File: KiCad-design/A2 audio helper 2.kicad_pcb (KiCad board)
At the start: 2 copper layers, 45.5 x 65.5 mm, 34 parts, among them J1 PIN HEADER 1x2, J10 PIN HEADER 1x2, J11 PIN HEADER 1x3, J12 PIN HEADER 1x3, J13 PIN HEADER 1x3, J2 PIN HEADER 1x2, J3 PIN HEADER 1x2, J4 SJ1-3515N, J5 PIN HEADER 1x3, J6 PIN HEADER 1x3, J7 SJ1-3515N, J8 PIN HEADER 1x5, J9 PIN HEADER 1x2, K1 SR11-5V-200-2C, SW2 SW_DPDT_x2, U1 pam8403

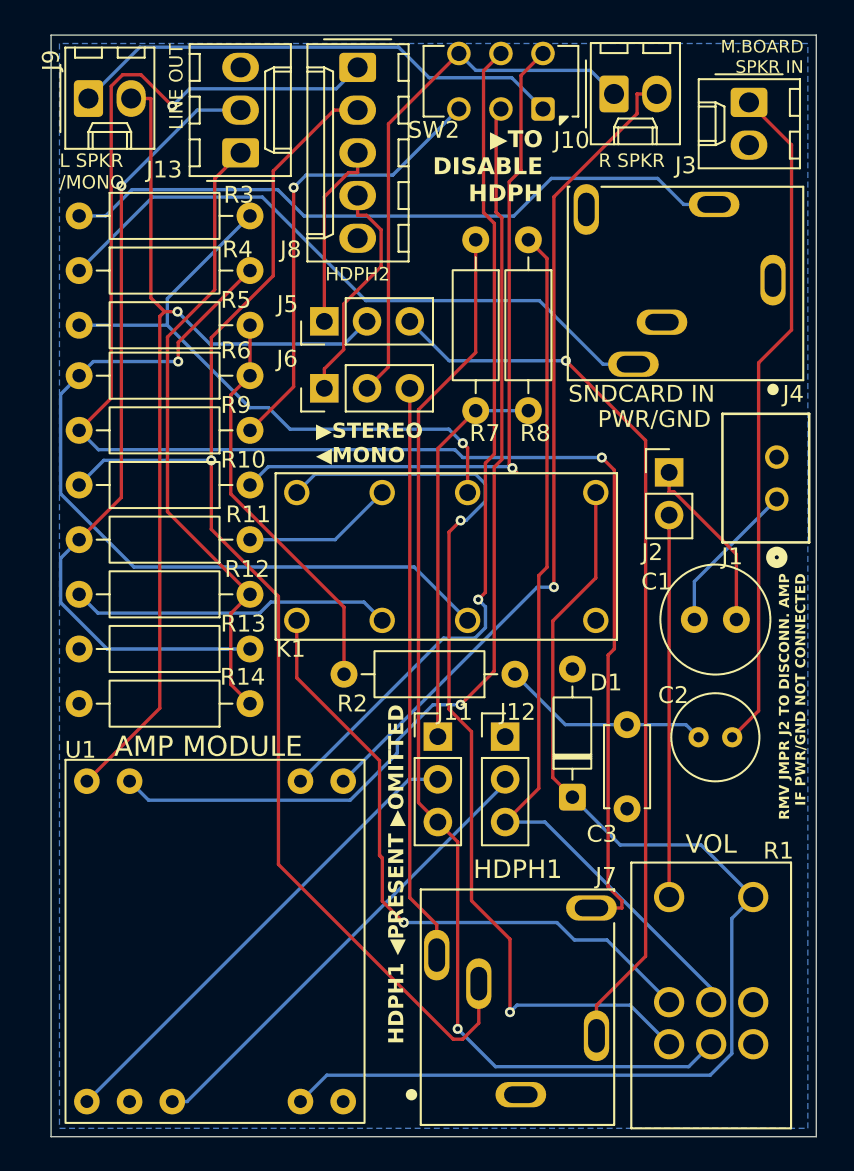
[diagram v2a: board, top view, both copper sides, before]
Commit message: ribbon cbl to remote vol & headph board
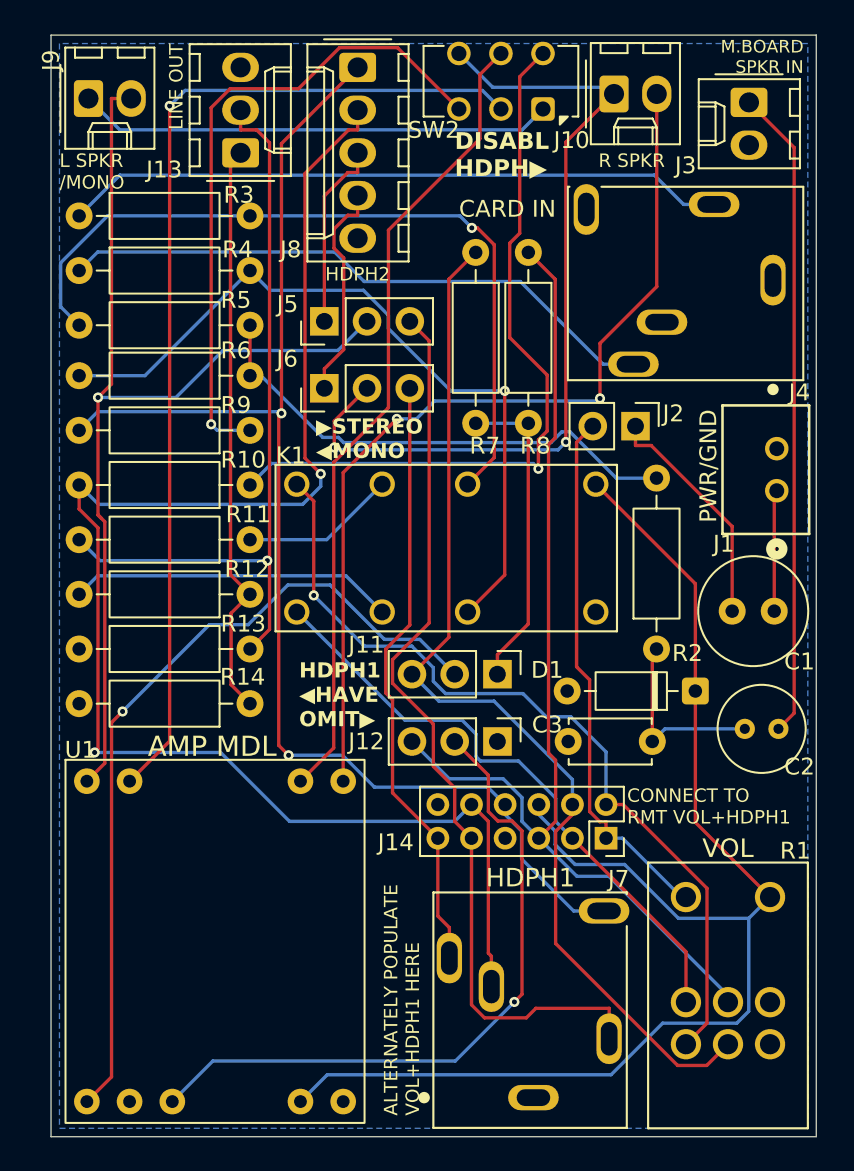
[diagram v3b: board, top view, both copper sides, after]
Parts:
- added J14: PIN HEADER 2x6, Connector_PinSocket_2.00mm:PinSocket_2x06_P2.00mm_Vertical, F.Cu at (83.0, 97.8)
- J1: footprint footprints:CONN_22035025_MOL -> Molex5267:CONN_22035025_MOL
- moved D1 9.66 mm to (88.3, 89.0), turned to 180 degrees
- moved R2 8.55 mm to (86.0, 86.5), turned to 90 degrees
- moved J11 5.13 mm to (76.5, 88.0), turned to -90 degrees
- moved C1 4.78 mm to (93.0, 84.2), turned to 180 degrees
- moved J2 3.40 mm to (84.8, 73.2), turned to -90 degrees
- moved C2 2.80 mm to (93.2, 91.2)
- moved C3 1.80 mm to (85.8, 92.0), turned to 180 degrees
- moved R1 1.00 mm to (90.2, 107.5)
- moved J7 0.77 mm to (78.7, 113.2)
- moved R7 0.75 mm to (75.2, 62.9)
- moved R8 0.75 mm to (78.4, 62.9)
- moved J12 0.54 mm to (76.5, 92.0), turned to -90 degrees
- moved J1 0.50 mm to (93.2, 77.1)
- moved K1 0.50 mm to (73.5, 80.5)
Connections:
- net /AMP_CONTROL renamed V_OUT
- net /HP1_IS_PRIMARY_L renamed HP1_TN
- net /HP1_IS_PRIMARY_R renamed HP1_RN
- net /HP_OUT_L renamed HP1_T
- net /HP_OUT_R renamed HP1_R
- net /VOLUME_ADJUSTED_L renamed VOL_L
- net /VOLUME_ADJUSTED_R renamed VOL_R
- net /VOLUME_SOURCE_L renamed SRC_L
- net /VOLUME_SOURCE_R renamed SRC_R
- net /V_IN_ENABLED renamed V_IN
- net GND renamed RMT_GND
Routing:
- net /AMP_INPUT_L: track 28.8 -> 49.1 mm, vias 0 -> 1
- net HP1_T: track 99.1 -> 79.5 mm
- net /RSPKR+: track 32.4 -> 50.5 mm, vias 0 -> 2
- net HP1_R: track 78.3 -> 91.9 mm, vias 1 -> 2
- net /AMP_INPUT_R: track 27.9 -> 40.6 mm, vias 0 -> 1
- net Net-(SW2A-C): track 27.3 -> 39.0 mm
- net V_OUT: track 69.5 -> 81.1 mm
- net /INPUT_AUDIO_L: track 37.3 -> 46.7 mm
- net V_IN: track 22.7 -> 32.0 mm
- net VOL_R: track 53.3 -> 62.5 mm
- net SRC_L: track 56.5 -> 49.7 mm, vias 2 -> 1
- net /AUDIO_MB_AC: track 24.0 -> 30.2 mm
- net /RSPKR-: track 49.9 -> 54.9 mm, vias 1 -> 2
- net /MONO_MIX_POINT: track 23.4 -> 18.8 mm
- net /LSPKR-: track 57.4 -> 60.8 mm
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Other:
- board text added: "ALTERNATELY POPULATE VOL+HDPH1 HERE"
- board text added: "AMP MDL"
- board text added: "CARD IN"
- board text added: "CONNECT TO RMT VOL+HDPH1"
- board text added: "HDPH1 ◀HAVE ︎OMIT▶"
- board text added: "︎︎DISABL HDPH▶"
- board text removed: "AMP MODULE"
- board text removed: "HDPH1 ◀︎PRESENT ▶︎OMITTED"
- board text removed: "RMV JMPR J2 TO DISCONN. AMP IF PWR/GND NOT CONNECTED"
- board text removed: "SNDCARD IN"
- board text removed: "▶︎︎TO DISABLE HDPH"

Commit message: desc'd ribbon conn better in schematic, fixed LSPKR+ error
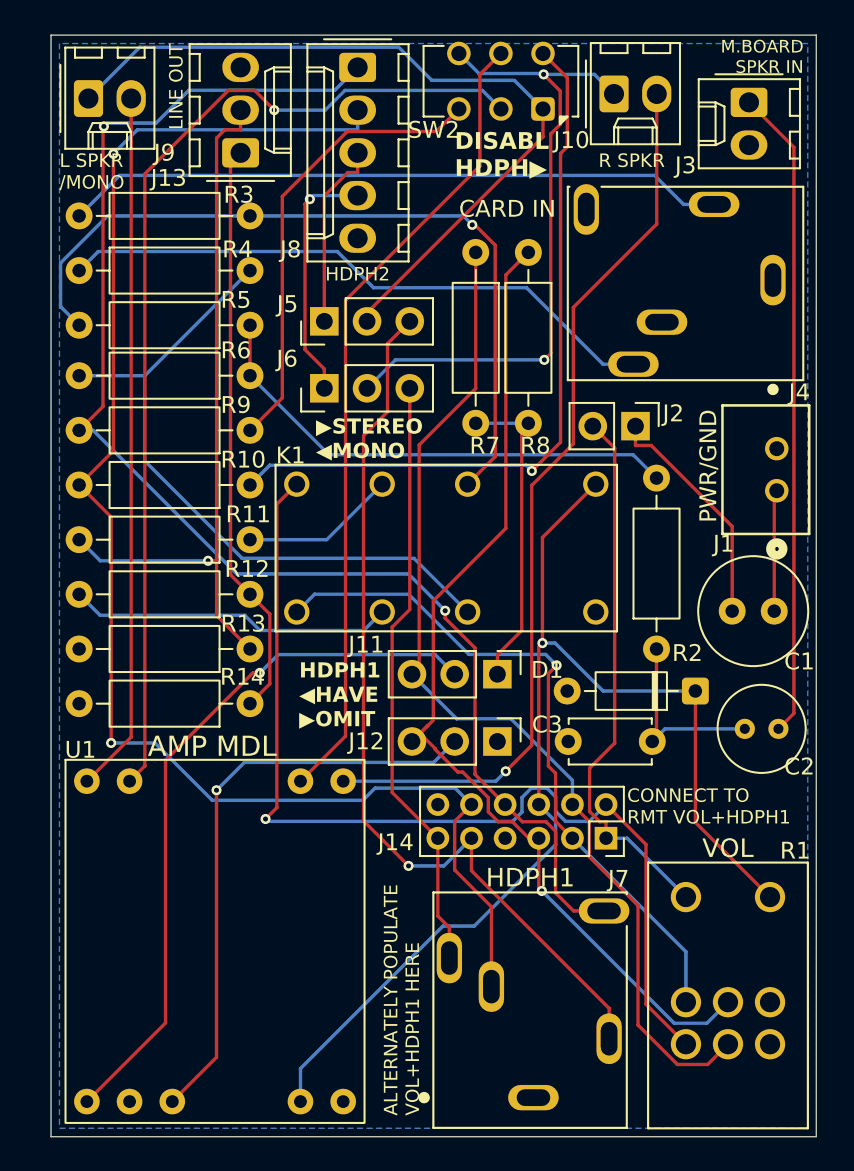
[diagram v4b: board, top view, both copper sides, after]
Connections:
- J5 pad 2: /LSPKR- -> /LSPKR+
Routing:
- net /LSPKR-: track 60.8 -> 41.7 mm, vias 1 -> 0
- net /LSPKR+: track 28.3 -> 46.8 mm
- net Net-(SW2A-C): track 39.0 -> 27.4 mm, vias 1 -> 0
- net /RSPKR+: track 50.5 -> 39.2 mm
- net V_OUT: track 81.1 -> 70.3 mm, vias 0 -> 1
- net SRC_L: track 49.7 -> 60.3 mm
- net /AMP_INPUT_L: track 49.1 -> 42.5 mm
- net /AMP_INPUT_R: track 40.6 -> 35.0 mm
- net HP1_T: track 79.5 -> 85.1 mm
- net SRC_R: track 36.1 -> 41.3 mm, vias 0 -> 1
- net /INPUT_AUDIO_R: track 45.4 -> 40.7 mm, vias 1 -> 0
- net HP1_R: track 91.9 -> 88.6 mm
- net /LINE_OUT_R: track 45.6 -> 42.7 mm
- net VOL_R: track 62.5 -> 60.8 mm, vias 0 -> 1
- net /HP2_IS_PRIMARY_R: track 13.1 -> 14.8 mm, vias 0 -> 1
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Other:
- board text added: "HDPH1 ◀HAVE ︎▶OMIT"
- board text removed: "HDPH1 ◀HAVE ︎OMIT▶"

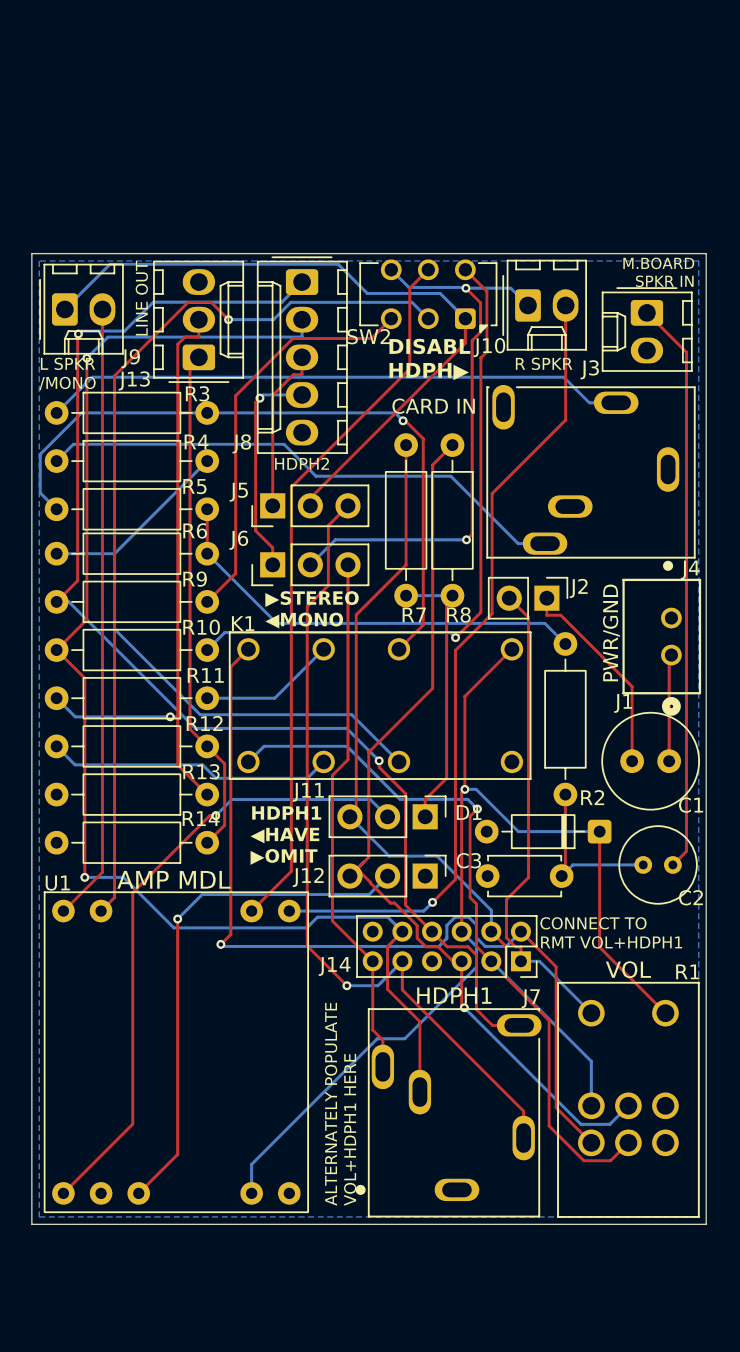
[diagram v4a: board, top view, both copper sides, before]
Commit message: daughtercard pcb, for now connected & perforated
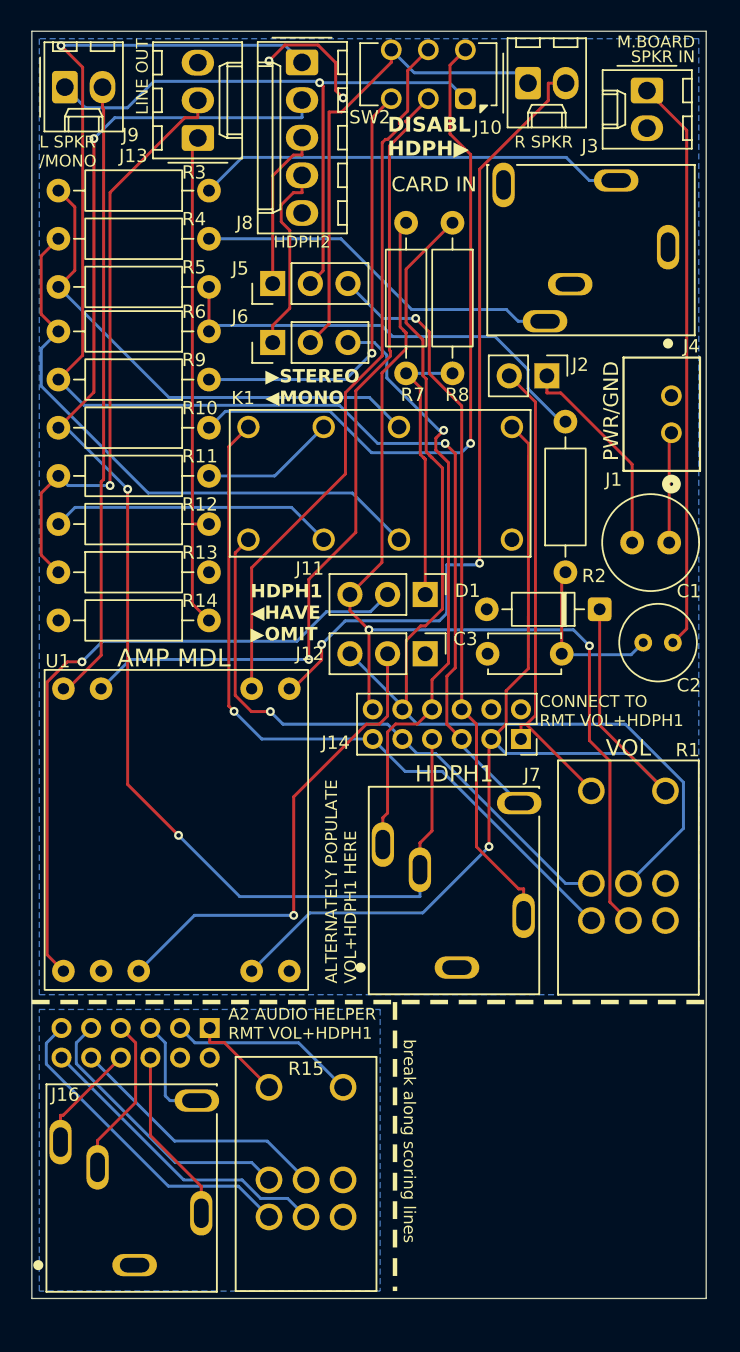
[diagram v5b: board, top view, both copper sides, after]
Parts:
- added J15: PIN HEADER 2x6, Connector_PinSocket_2.00mm:PinSocket_2x06_P2.00mm_Vertical, B.Cu at (62.0, 102.2)
- added J16: SJ1-3515N, SJ1-3515N:CUI_SJ1-3515N, F.Cu at (56.9, 118.2)
- added R15: 10kΩ, PTR902-1020K-A502:TRIM_PTR902-1020K-A502, F.Cu at (68.5, 112.5)
- moved R3 18.2 mm to (62.0, 45.8), turned to 180 degrees
- moved R4 18.2 mm to (62.0, 49.0), turned to 180 degrees
- moved R13 18.0 mm to (51.8, 71.5), turned to 0 degrees
- moved R10 15.0 mm to (62.0, 61.8)
- moved R11 15.0 mm to (62.0, 65.0)
- moved R12 15.0 mm to (62.0, 68.2)
- moved R14 15.0 mm to (62.0, 74.8)
- moved R5 15.0 mm to (62.0, 52.2)
- moved R6 15.0 mm to (62.0, 55.2)
- moved R9 15.0 mm to (62.0, 58.5)
- moved J1 15.0 mm to (93.2, 62.1)
- moved C2 15.0 mm to (93.2, 76.2)
- moved C3 15.0 mm to (85.8, 77.0)
- moved D1 15.0 mm to (88.3, 74.0)
- moved J10 15.0 mm to (83.5, 38.5)
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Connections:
- C3 pad 2: RMT_GND -> GND
- D1 pad 2: RMT_GND -> GND
- J1 pad 2: RMT_GND -> GND
- J12 pad 1: RMT_GND -> GND
- J13 pad 3: RMT_GND -> GND
- J14 pad 10: HP1_R -> VOL_R
- J14 pad 11: HP1_RN -> SRC_L
- J14 pad 12: unconnected-(J14-Pin_12-Pad12) -> VOL_L
- J14 pad 2: SRC_L -> GND
- J14 pad 3: SRC_R -> V_OUT
- J14 pad 4: VOL_L -> unconnected-(J14-Pin_4-Pad4)
- J14 pad 5: VOL_R -> HP1_T
- J14 pad 6: V_OUT -> HP1_TN
- J14 pad 7: RMT_GND -> HP1_R
- J14 pad 8: HP1_T -> HP1_RN
- J14 pad 9: HP1_TN -> SRC_R
- J3 pad 2: RMT_GND -> GND
- J4 pad 1: RMT_GND -> GND
- J4 pad 4: RMT_GND -> GND
- J4 pad 5: RMT_GND -> GND
- J7 pad 1: RMT_GND -> GND
- J8 pad 5: RMT_GND -> GND
- K1 pad A2: RMT_GND -> GND
- R1 pad R1_3: RMT_GND -> GND
- R1 pad R2_3: RMT_GND -> GND
- R13 pad 2: RMT_GND -> GND
- R14 pad 2: RMT_GND -> GND
- U1 pad 5: RMT_GND -> GND
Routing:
- net /Daughterboard/RMT_SRC_L: track 0.00 -> 22.2 mm
- net /Daughterboard/REM_VOL_L: track 0.00 -> 21.0 mm
- net /Daughterboard/RMT_SRC_R: track 0.00 -> 19.1 mm
- net /Daughterboard/REM_VOL_R: track 0.00 -> 17.9 mm
- net /Daughterboard/RMT_V_OUT: track 0.00 -> 12.7 mm
- net /INPUT_AUDIO_L: track 46.8 -> 34.3 mm, vias 1 -> 0
- net /Daughterboard/RMT_HP1_TN: track 0.00 -> 11.9 mm
- net /JACK_R: track 36.2 -> 25.0 mm
- net /Daughterboard/RMT_HP1_R: track 0.00 -> 10.9 mm
- net VOL_R: track 60.8 -> 71.3 mm, vias 1 -> 0
- net SRC_L: track 60.3 -> 49.8 mm
- net /JACK_L: track 39.5 -> 29.0 mm
- net HP1_T: track 85.1 -> 95.2 mm
- net VOL_L: track 61.8 -> 70.6 mm, vias 0 -> 2
- net GND: track 0.00 -> 8.02 mm, vias 0 -> 2
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- added copper zone on B.Cu, net GND
- added copper zone on B.Cu, net GND2
- removed copper zone on B.Cu, net RMT_GND
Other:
- board size 45.5 x 65.5 mm -> 45.5 x 85.5 mm
- board text added: "A2 AUDIO HELPER RMT VOL+HDPH1"
- board text added: "Apple 2 Audio Helper v0.8"
- board text added: "M.BOARD"
- board text added: "SPKR IN"
- board text added: "break along scoring lines"
- board text removed: "Apple 2 Audio Helper v0.7"
- board text removed: "M.BOARD SPKR IN"
